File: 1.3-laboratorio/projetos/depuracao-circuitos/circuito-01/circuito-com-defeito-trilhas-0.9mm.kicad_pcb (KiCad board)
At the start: 2 copper layers, 76.2 x 54.6 mm, 26 parts, among them J1 Conn_01x07_Male, J2 Conn_01x07_Male, J3 Conn_01x07_Male, J4 Conn_01x07_Male, J5 Conn_01x07_Male, J6 Conn_01x07_Male, J7 Conn_01x05, J8 Conn_01x05, P1 CONN_01X02, SW1 SW_DIP_x04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

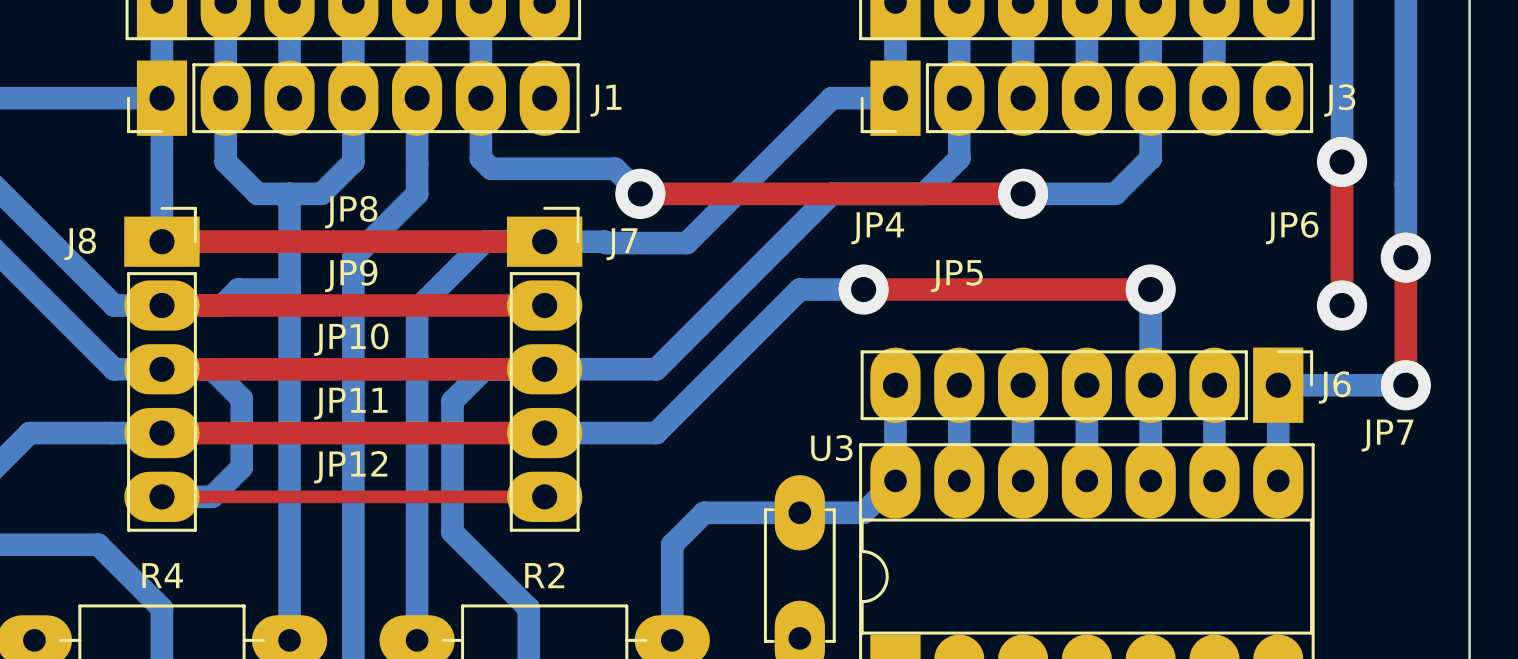
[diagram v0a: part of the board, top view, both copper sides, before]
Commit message: Via próxima a ilha movida.
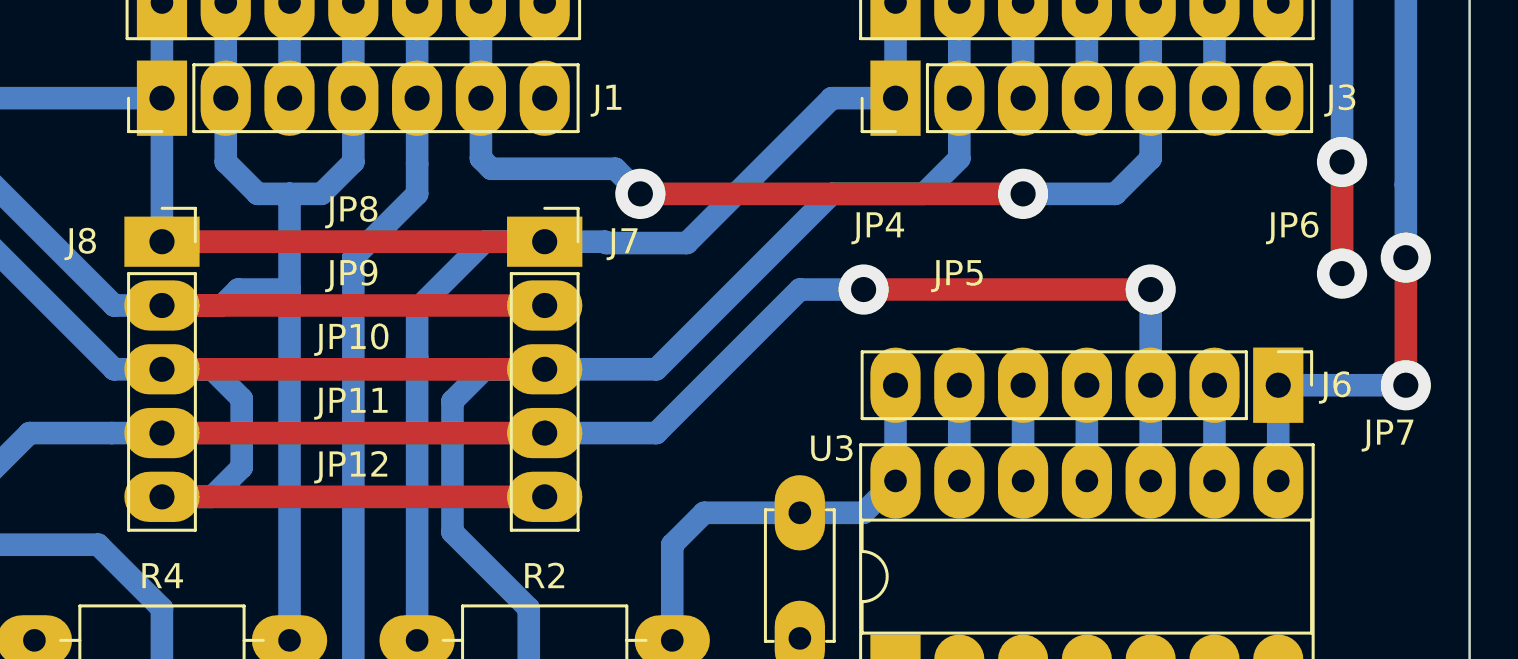
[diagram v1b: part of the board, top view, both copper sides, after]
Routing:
- net /U2-08: track 24.5 -> 23.3 mm
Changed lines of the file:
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@@
     (user_trace_width 1)
     (trace_clearance 0.508)
-    (zone_clearance 0.508)
+    (zone_clearance 0.9)
     (zone_45_only no)
     (trace_min 0.9)
@@
   (gr_line (start 182.88 71.12) (end 182.88 123.19) (angle 90) (layer Margin) (width 0.2))
   (gr_line (start 109.22 71.12) (end 182.88 71.12) (angle 90) (layer Margin) (width 0.2))
-  (segment (start 134.08 108.585) (end 147.32 108.585) (width 0.5) (layer F.Cu) (net 1))
-  (segment (start 132.08 108.585) (end 134.08 108.585) (width 0.5) (layer F.Cu) (net 1))
+  (segment (start 134.08 108.585) (end 147.32 108.585) (width 0.9) (layer F.Cu) (net 1))
+  (segment (start 132.08 108.585) (end 134.08 108.585) (width 0.9) (layer F.Cu) (net 1))
   (segment (start 114.94 116.205) (end 116.84 116.205) (width 0.9) (layer B.Cu) (net 2))
   (segment (start 113.03 114.295) (end 114.94 116.205) (width 0.9) (layer B.Cu) (net 2))
@@
   (segment (start 176.53 81.28) (end 176.53 83.28) (width 0.9) (layer B.Cu) (net 6) (status 10))
   (segment (start 176.53 83.28) (end 179.07 85.82) (width 0.9) (layer B.Cu) (net 6))
-  (via (at 179.07 100.965) (size 2) (drill 1) (layers F.Cu B.Cu) (net 6))
-  (segment (start 179.07 95.25) (end 179.07 100.965) (width 0.9) (layer F.Cu) (net 6))
+  (segment (start 179.07 95.25) (end 179.07 99.695) (width 0.9) (layer F.Cu) (net 6))
+  (via (at 179.07 99.695) (size 2) (drill 1) (layers F.Cu B.Cu) (net 6))
   (segment (start 173.99 119.38) (end 173.99 115.57) (width 0.9) (layer B.Cu) (net 7) (status 30))
   (segment (start 171.45 115.57) (end 171.45 119.38) (width 0.9) (layer B.Cu) (net 8) (status 30))
